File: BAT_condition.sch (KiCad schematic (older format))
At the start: 2 parts

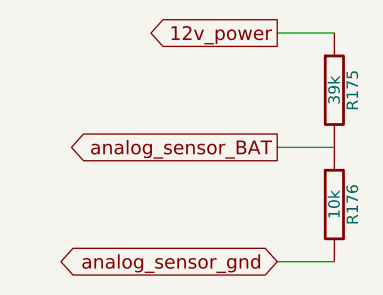
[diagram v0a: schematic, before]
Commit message: DFH mans up a bit. Perhaps usable for something at this point, like making trips to the local store ;)
I connected TA pins to sub circuits, fixed a number if items discussed in the DIYEFI forums. This is it's 21st version, so it was time for it to man up a bit, and become something potentially useful.

Signed-off-by: Jared Harvey <TortiseGIT@jaredharvey.com>
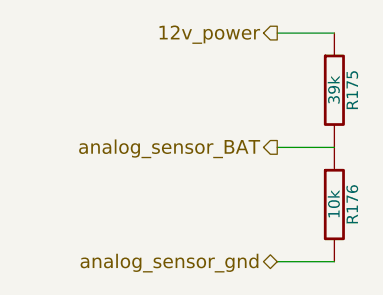
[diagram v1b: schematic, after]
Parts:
- R175: Field10 (none) -> carbon film; Field11 (none) -> other,more,stuff; Field4 (none) -> newark,38K0371; Field5 (none) -> vendor1, smd w hem; Field6 (none) -> vendor2, thru w hem; Field7 (none) -> vendor2, smd w hem; Field8 (none) -> 250,mW; Field9 (none) -> 5,%
- R176: Field10 (none) -> carbon film; Field11 (none) -> other,more,stuff; Field4 (none) -> newark,38k0328; Field5 (none) -> vendor1, smd w hem; Field6 (none) -> vendor2, thru w hem; Field7 (none) -> vendor2, smd w hem; Field8 (none) -> 250,mW; Field9 (none) -> 5,%
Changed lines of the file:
@@
-EESchema Schematic File Version 1
-LIBS:power,./freeEMS_lib,device,conn,linear,regul,74xx,cmos4000,adc-dac,memory,xilinx,special,microcontrollers,dsp,microchip,analog_switches,motorola,texas,intel,audio,interface,digital-audio,philips,display,cypress,siliconi,contrib,valves,./freeEMS_1.cache
-EELAYER 23  0
+EESchema Schematic File Version 2  date 9/10/2011 11:43:52 AM
+LIBS:power
+LIBS:freeEMS_lib
+LIBS:device
+LIBS:conn
+LIBS:linear
+LIBS:regul
+LIBS:74xx
+LIBS:cmos4000
+LIBS:adc-dac
+LIBS:memory
+LIBS:xilinx
+LIBS:special
+LIBS:microcontrollers
+LIBS:dsp
+LIBS:microchip
+LIBS:analog_switches
+LIBS:motorola
+LIBS:texas
+LIBS:intel
+LIBS:audio
+LIBS:interface
+LIBS:digital-audio
+LIBS:philips
+LIBS:display
+LIBS:cypress
+LIBS:siliconi
+LIBS:contrib
+LIBS:valves
+LIBS:freeEMS_1-cache
+EELAYER 25  0
 EELAYER END
 $Descr A4 11700 8267
+encoding utf-8
 Sheet 37 41
-Title "freeEMS 1.0"
-Date "15 nov 2008"
-Rev "A.20"
-Comp "diyefi.org"
+Title "DFH for freeEMS"
+Date "10 sep 2011"
+Rev "A.21"
+Comp "FreeEMS.org"
 Comment1 "BAT_condition"
 Comment2 ""
@@
 Wire Wire Line
 	2250 2300 2500 2300
-Text GLabel 2250 1800 0    60   Output
+Text HLabel 2250 1800 0    60   Output ~ 0
 12v_power
 $Comp
@@
 U 1 1 4890FC9B
 P 2500 2550
-F 0 "R176" V 2580 2550 50  0000 C C
-F 1 "10k" V 2500 2550 50  0000 C C
-F 2 "R4-SM0805" V 2680 2650 60  0001 C C
-F 4 "newark,38k0328" V 1130 2600 60  0001 C C
-F 5 "vendor1, smd w hem" V 1130 2600 60  0001 C C
-F 6 "vendor2, thru w hem" V 1130 2600 60  0001 C C
-F 7 "vendor2, smd w hem" V 1130 2600 60  0001 C C
-F 8 "250,mW" V 1130 2600 60  0001 C C
-F 9 "5,%" V 1130 2600 60  0001 C C
-F 10 "carbon film" V 1130 2600 60  0001 C C
-F 11 "other,more,stuff" V 1130 2600 60  0001 C C
+F 0 "R176" V 2580 2550 50  0000 C CNN
+F 1 "10k" V 2500 2550 50  0000 C CNN
+F 2 "R4-SM0805" V 2680 2650 60  0001 C CNN
+F 4 "newark,38k0328" V 1130 2600 60  0001 C CNN "Field4"
+F 5 "vendor1, smd w hem" V 1130 2600 60  0001 C CNN "Field5"
+F 6 "vendor2, thru w hem" V 1130 2600 60  0001 C CNN "Field6"
+F 7 "vendor2, smd w hem" V 1130 2600 60  0001 C CNN "Field7"
+F 8 "250,mW" V 1130 2600 60  0001 C CNN "Field8"
+F 9 "5,%" V 1130 2600 60  0001 C CNN "Field9"
+F 10 "carbon film" V 1130 2600 60  0001 C CNN "Field10"
+F 11 "other,more,stuff" V 1130 2600 60  0001 C CNN "Field11"
 	1    2500 2550
 	1    0    0    -1
@@
 U 1 1 4890FC93
 P 2500 2050
-F 0 "R175" V 2580 2050 50  0000 C C
-F 1 "39k" V 2500 2050 50  0000 C C
-F 2 "R4-SM0805" V 2680 2150 60  0001 C C
-F 4 "newark,38K0371" V 1130 2600 60  0001 C C
-F 5 "vendor1, smd w hem" V 1130 2600 60  0001 C C
-F 6 "vendor2, thru w hem" V 1130 2600 60  0001 C C
-F 7 "vendor2, smd w hem" V 1130 2600 60  0001 C C
-F 8 "250,mW" V 1130 2600 60  0001 C C
-F 9 "5,%" V 1130 2600 60  0001 C C
-F 10 "carbon film" V 1130 2600 60  0001 C C
-F 11 "other,more,stuff" V 1130 2600 60  0001 C C
+F 0 "R175" V 2580 2050 50  0000 C CNN
+F 1 "39k" V 2500 2050 50  0000 C CNN
+F 2 "R4-SM0805" V 2680 2150 60  0001 C CNN
+F 4 "newark,38K0371" V 1130 2600 60  0001 C CNN "Field4"
+F 5 "vendor1, smd w hem" V 1130 2600 60  0001 C CNN "Field5"
+F 6 "vendor2, thru w hem" V 1130 2600 60  0001 C CNN "Field6"
+F 7 "vendor2, smd w hem" V 1130 2600 60  0001 C CNN "Field7"
+F 8 "250,mW" V 1130 2600 60  0001 C CNN "Field8"
+F 9 "5,%" V 1130 2600 60  0001 C CNN "Field9"
+F 10 "carbon film" V 1130 2600 60  0001 C CNN "Field10"
+F 11 "other,more,stuff" V 1130 2600 60  0001 C CNN "Field11"
 	1    2500 2050
 	1    0    0    -1
 $EndComp
-Text GLabel 2250 2800 0    60   BiDi
+Text HLabel 2250 2800 0    60   BiDi ~ 0
 analog_sensor_gnd
-Text GLabel 2250 2300 0    60   Output
+Text HLabel 2250 2300 0    60   Output ~ 0
 analog_sensor_BAT
 $EndSCHEMATC
